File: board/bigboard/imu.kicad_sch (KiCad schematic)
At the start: 6 parts, among them U8 BMM150, U9 BMI270

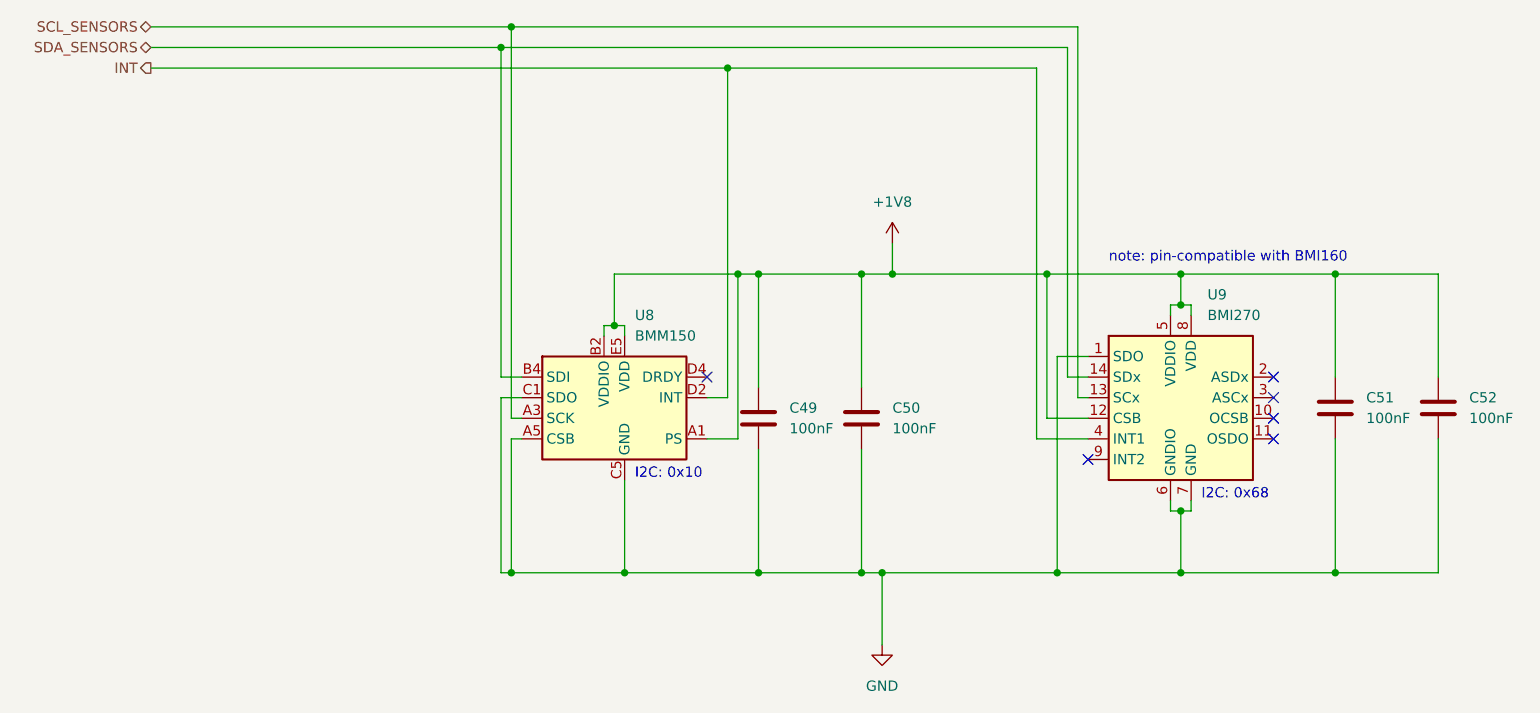
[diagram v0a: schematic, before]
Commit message: Manufactured version of bigboard
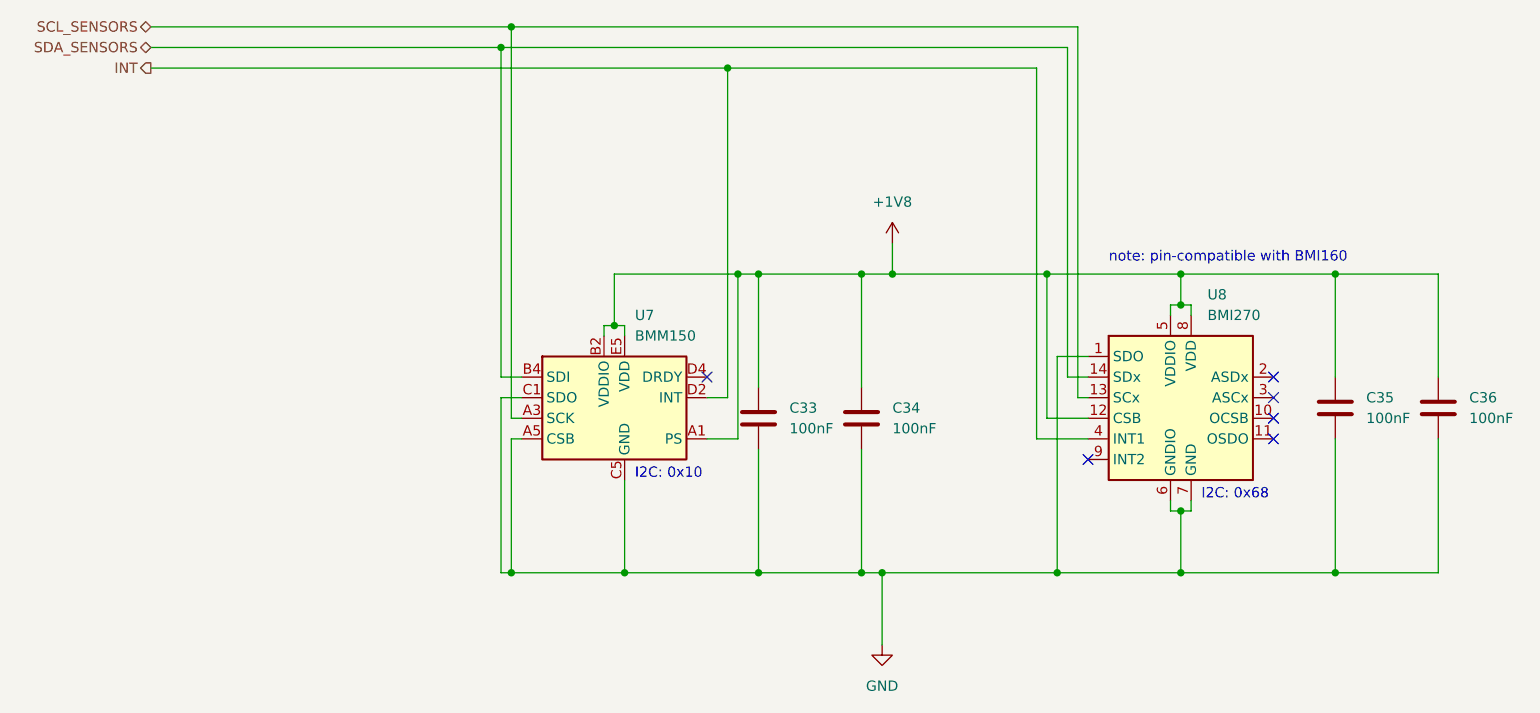
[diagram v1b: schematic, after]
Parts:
- C33: renamed from C49; MPN (none) -> CC0201KRX5R8BB104
- C34: renamed from C50; MPN (none) -> CC0201KRX5R8BB104
- C35: renamed from C51; MPN (none) -> CC0201KRX5R8BB104
- C36: renamed from C52; MPN (none) -> CC0201KRX5R8BB104
- renumbered U8 to U7, U9 to U8
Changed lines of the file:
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@@
   (symbol (lib_id "Sensor_Motion:BMI160") (at 190.5 107.95 0) (unit 1)
     (in_bom yes) (on_board yes)
-    (property "Reference" "U9" (id 0) (at 192.5194 95.25 0)
+    (property "Reference" "U8" (id 0) (at 192.5194 95.25 0)
       (effects (font (size 1.27 1.27)) (justify left))
     )
@@
   (symbol (lib_id "Device:C") (at 220.98 109.22 0) (unit 1)
     (in_bom yes) (on_board yes) (fields_autoplaced)
-    (property "Reference" "C52" (id 0) (at 224.79 107.9499 0)
+    (property "Reference" "C36" (id 0) (at 224.79 107.9499 0)
       (effects (font (size 1.27 1.27)) (justify left))
     )
@@
       (effects (font (size 1.27 1.27)) hide)
     )
+    (property "MPN" "CC0201KRX5R8BB104" (id 5) (at 220.98 109.22 0)
+      (effects (font (size 1.27 1.27)) hide)
+    )
     (pin "1")
     (pin "2")
@@
   (symbol (lib_id "Sensor_Magnetic:BMM150") (at 120.65 107.95 0) (unit 1)
     (in_bom yes) (on_board yes)
-    (property "Reference" "U8" (id 0) (at 121.92 97.79 0)
+    (property "Reference" "U7" (id 0) (at 121.92 97.79 0)
       (effects (font (size 1.27 1.27)) (justify left))
     )
@@
   (symbol (lib_id "Device:C") (at 137.16 110.49 0) (unit 1)
     (in_bom yes) (on_board yes)
-    (property "Reference" "C49" (id 0) (at 140.97 109.2199 0)
+    (property "Reference" "C33" (id 0) (at 140.97 109.2199 0)
       (effects (font (size 1.27 1.27)) (justify left))
     )
@@
       (effects (font (size 1.27 1.27)) hide)
     )
+    (property "MPN" "CC0201KRX5R8BB104" (id 5) (at 137.16 110.49 0)
+      (effects (font (size 1.27 1.27)) hide)
+    )
     (pin "1")
     (pin "2")
@@
   (symbol (lib_id "power:+1V8") (at 153.67 88.9 0) (unit 1)
     (in_bom yes) (on_board yes) (fields_autoplaced)
-    (property "Reference" "#PWR040" (id 0) (at 153.67 92.71 0)
+    (property "Reference" "#PWR036" (id 0) (at 153.67 92.71 0)
       (effects (font (size 1.27 1.27)) hide)
     )
@@
   (symbol (lib_id "Device:C") (at 149.86 110.49 0) (unit 1)
     (in_bom yes) (on_board yes) (fields_autoplaced)
-    (property "Reference" "C50" (id 0) (at 153.67 109.2199 0)
+    (property "Reference" "C34" (id 0) (at 153.67 109.2199 0)
       (effects (font (size 1.27 1.27)) (justify left))
     )
@@
       (effects (font (size 1.27 1.27)) hide)
     )
+    (property "MPN" "CC0201KRX5R8BB104" (id 5) (at 149.86 110.49 0)
+      (effects (font (size 1.27 1.27)) hide)
+    )
     (pin "1")
     (pin "2")
@@
   (symbol (lib_id "power:GND") (at 152.4 138.43 0) (unit 1)
     (in_bom yes) (on_board yes) (fields_autoplaced)
-    (property "Reference" "#PWR039" (id 0) (at 152.4 144.78 0)
+    (property "Reference" "#PWR035" (id 0) (at 152.4 144.78 0)
       (effects (font (size 1.27 1.27)) hide)
     )
@@
   (symbol (lib_id "Device:C") (at 208.28 109.22 0) (unit 1)
     (in_bom yes) (on_board yes)
-    (property "Reference" "C51" (id 0) (at 212.09 107.9499 0)
+    (property "Reference" "C35" (id 0) (at 212.09 107.9499 0)
       (effects (font (size 1.27 1.27)) (justify left))
     )
@@
       (effects (font (size 1.27 1.27)) hide)
     )
+    (property "MPN" "CC0201KRX5R8BB104" (id 5) (at 208.28 109.22 0)
+      (effects (font (size 1.27 1.27)) hide)
+    )
